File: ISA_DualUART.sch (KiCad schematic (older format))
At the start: 46 parts, among them J1 ISA BUS, J2 ADDR_IRQ, J3 UART1_SEL, J4 UART2_SEL, J5 Serial 1 IDC, J6 Serial 2 IDC, J7 Serial 1 DB9, SW1 GP Address, U1 74LS138, U10 74LS32, U2 74LS138, U3 74LS32, U4 16550, U5 GD75232N, U6 GD75232N, U7 NE558, U8 74LS688, U9 74HC244, X1 1.8432Mhz

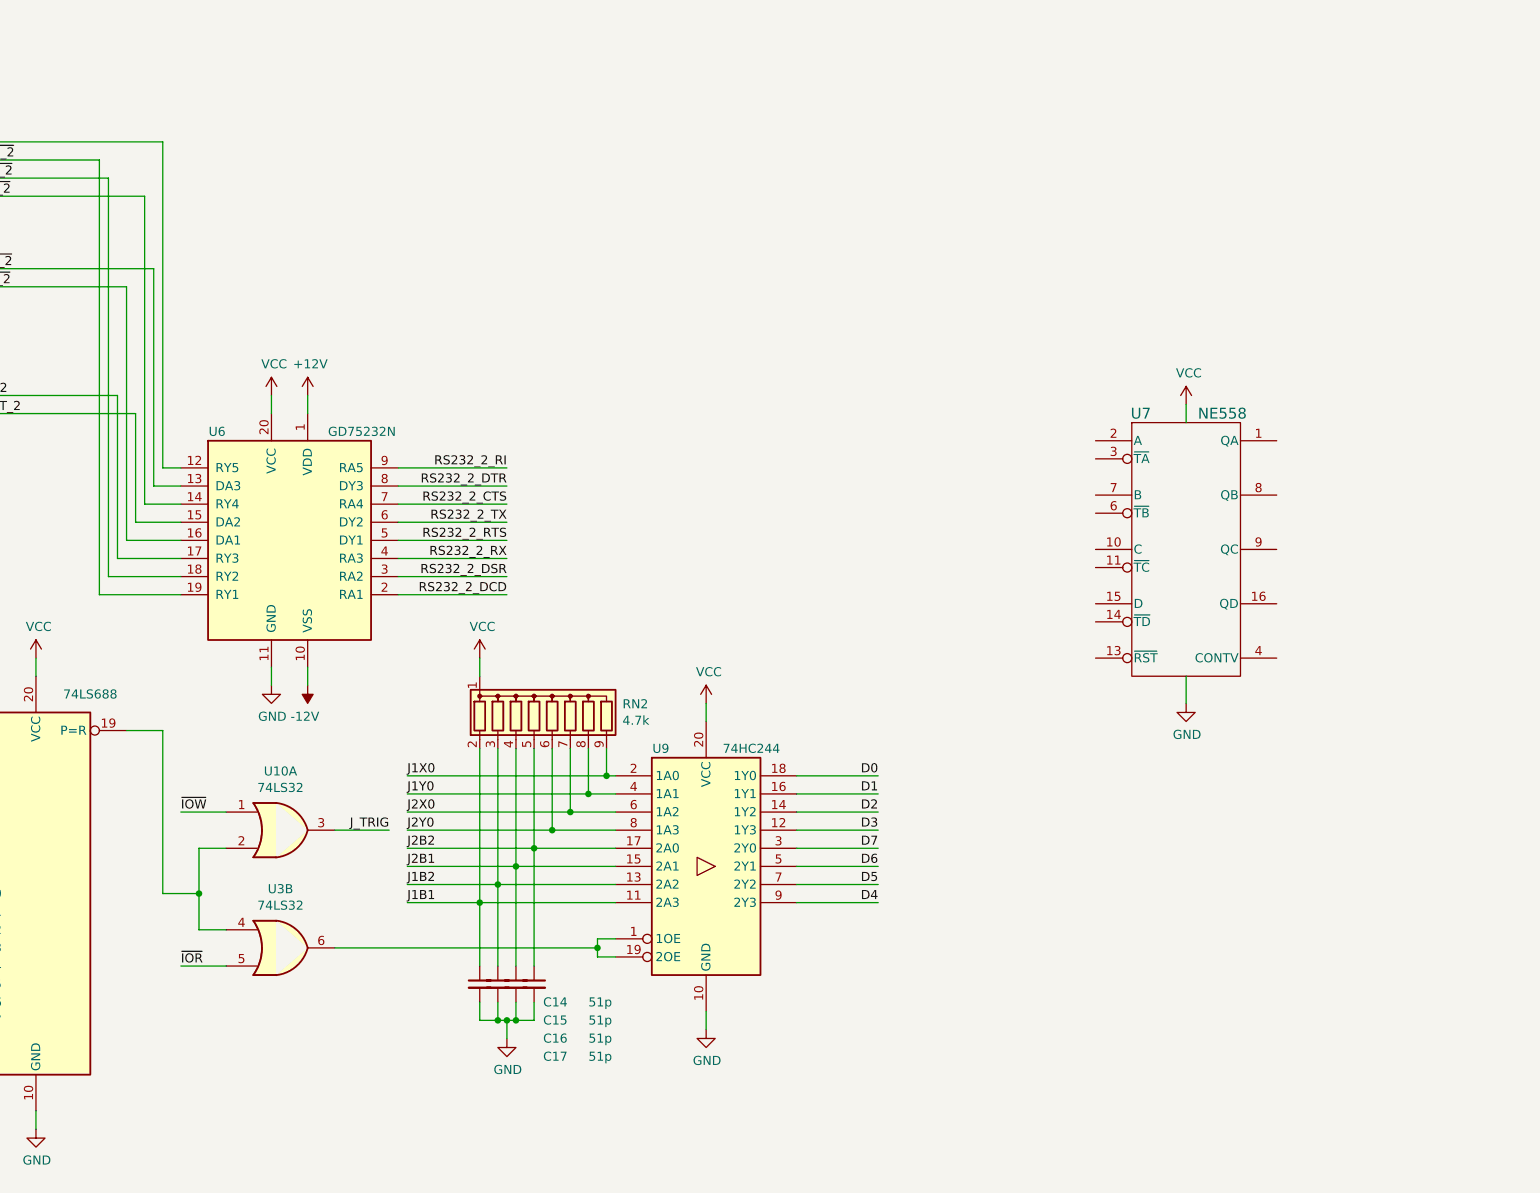
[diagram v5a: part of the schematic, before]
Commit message: Add gameport components
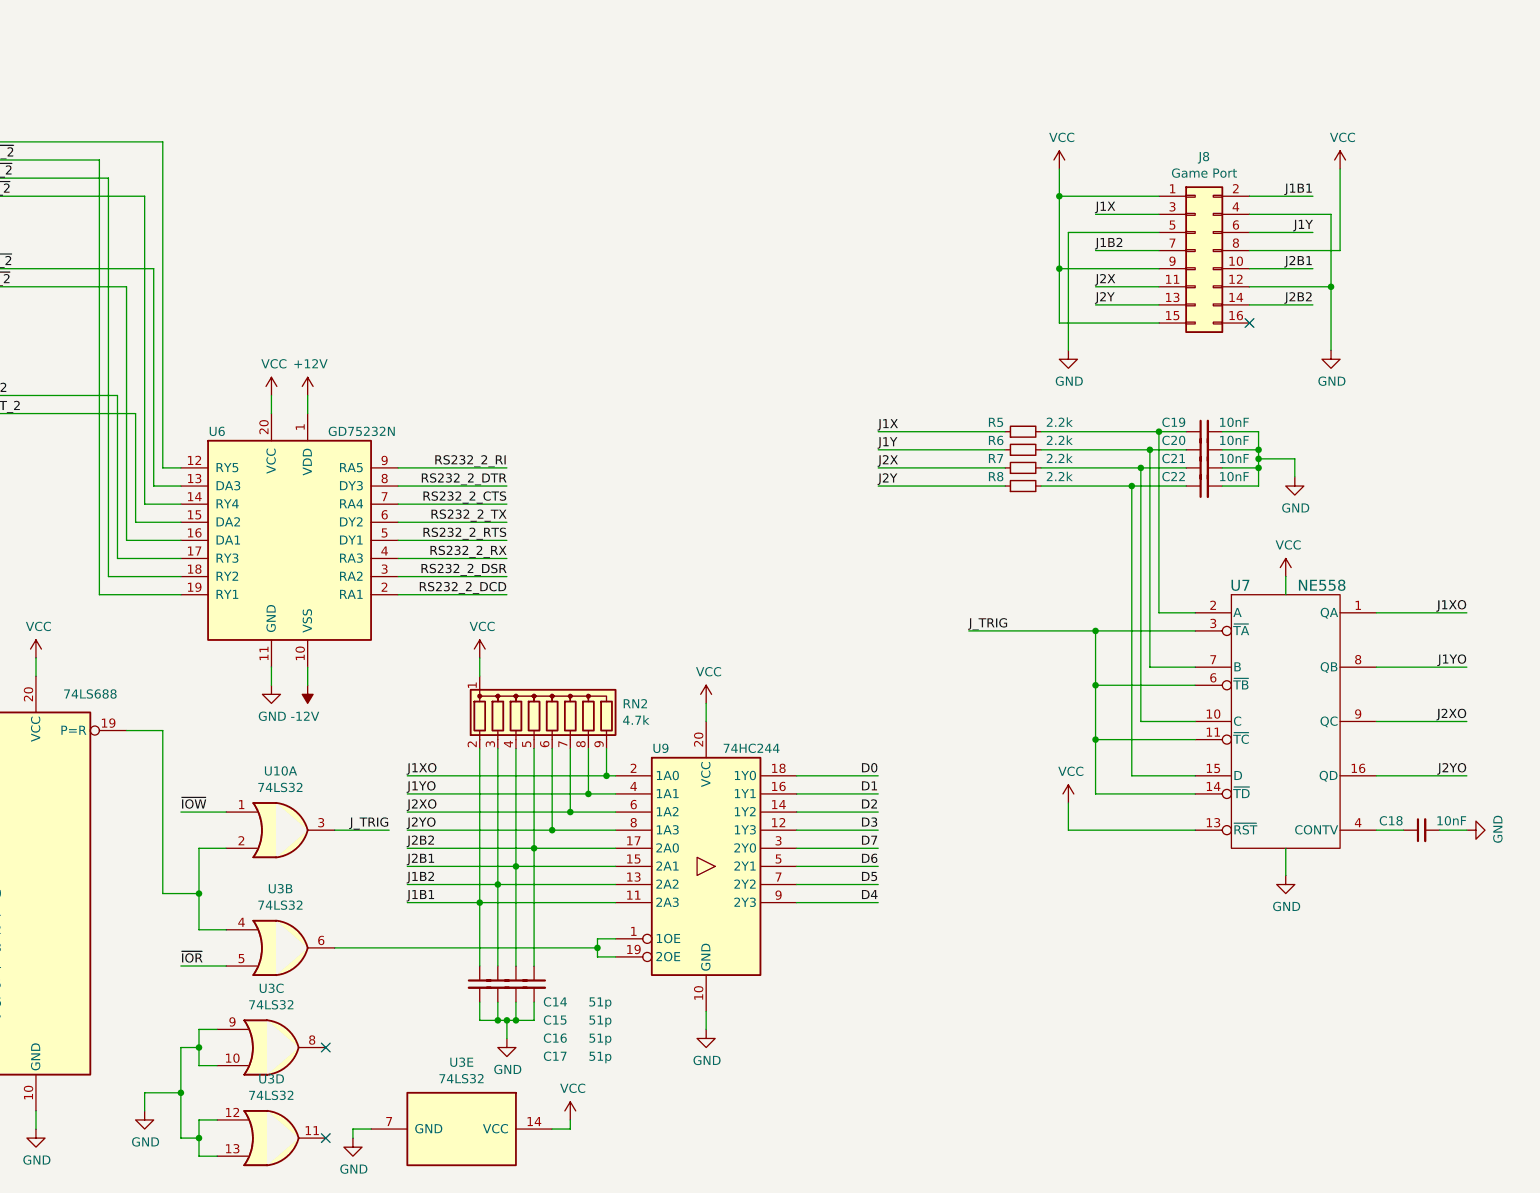
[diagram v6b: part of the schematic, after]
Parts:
- added C18, C19, C20, C21, C22: 10nF, Capacitor_THT:C_Disc_D5.0mm_W2.5mm_P2.50mm, symbol Device:C_Small
- added J8: Game Port, Connector_PinHeader_2.54mm:PinHeader_2x08_P2.54mm_Vertical, symbol Connector_Generic:Conn_02x08_Odd_Even
- added R5, R6, R7, R8: 2.2k, Resistor_THT:R_Axial_DIN0207_L6.3mm_D2.5mm_P10.16mm_Horizontal, symbol Device:R_Small
- added unit 3 of U3
- added unit 4 of U3
- added unit 5 of U3
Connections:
- net J1X0 is gone; now on net J1XO: RN2.9 (R8), U9.2 (1A0)
- net J1Y0 is gone; now on net J1YO: RN2.8 (R7), U9.4 (1A1)
- net J2X0 is gone; now on net J2XO: RN2.7 (R6), U9.6 (1A2)
- net J2Y0 is gone; now on net J2YO: RN2.6 (R5), U9.8 (1A3)
- net GND: now also C18.2, C19.2, C20.2, C21.2, C22.2, J8.12 (Pin_12), J8.4 (Pin_4), J8.5 (Pin_5), U3.10, U3.12, U3.13, U3.7 (GND), U3.9
- net J1B1: now also J8.2 (Pin_2)
- net J1B2: now also J8.7 (Pin_7)
- net J2B1: now also J8.10 (Pin_10)
- net J2B2: now also J8.14 (Pin_14)
- net J_TRIG: now also U7.11 (~TC), U7.14 (~TD), U7.3 (~TA), U7.6 (~TB)
- net VCC: now also U7.13 (~RST), J8.1 (Pin_1), J8.15 (Pin_15), J8.8 (Pin_8), J8.9 (Pin_9), U3.14 (VCC)
- net J1XO: now reaches U7.1 (QA)
- net at U7.10 (C): now also C21.1, R7.2
- net at U7.15 (D): now also C22.1, R8.2
- net J2YO: now reaches U7.16 (QD)
- net at U7.2 (A): now also C19.1, R5.2
- net at U7.4 (CONTV): now also C18.1
- net at U7.7 (B): now also C20.1, R6.2
- net J1YO: now reaches U7.8 (QB)
- net J2XO: now reaches U7.9 (QC)
- new net J1X: J8.3 (Pin_3), R5.1
- new net J1Y: J8.6 (Pin_6), R6.1
- new net J2X: J8.11 (Pin_11), R7.1
- new net J2Y: J8.13 (Pin_13), R8.1
- no-connect marks 39 -> 42
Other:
- moved on the sheet: U7

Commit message: Add more components of the parallel port
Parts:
- added C23, C24, C25, C26: 100nF, Capacitor_THT:C_Disc_D6.0mm_W2.5mm_P5.00mm, symbol Device:C_Small
- added C27, C28, C29, C30, C31, C32, C33, C34, C35: 2.2nF, Capacitor_THT:C_Disc_D5.0mm_W2.5mm_P5.00mm, symbol Device:C_Small
- added JP1: Address selection, Connector_PinHeader_2.54mm:PinHeader_1x02_P2.54mm_Vertical, symbol Device:Jumper_NO_Small
- added JP2: Parport type, Connector_PinHeader_2.54mm:PinHeader_1x03_P2.54mm_Vertical, symbol Device:Jumper_NC_Dual
- added R10, R11, R12, R13, R14, R9: 4.7k, Resistor_THT:R_Axial_DIN0207_L6.3mm_D2.5mm_P10.16mm_Horizontal, symbol Device:R_Small
- added U11: 74LS30, Package_DIP:DIP-14_W7.62mm_LongPads, symbol 74xx:74LS30
- added U12: 74LS86, Package_DIP:DIP-14_W7.62mm_LongPads, symbol 74xx:74LS86
- added U13: 74LS02, Package_DIP:DIP-14_W7.62mm_LongPads, symbol 74xx:74LS02
- added U14: 74LS155, Package_DIP:DIP-16_W7.62mm_LongPads, symbol 74xx:74LS155
- added U15: 74LS245, Package_DIP:DIP-20_W7.62mm_LongPads, symbol 74xx:74LS245
- added U16: 74LS174, Package_DIP:DIP-16_W7.62mm_Socket_LongPads, symbol 74xx:74LS174
- added U17: 74LS374, symbol 74xx:74LS374
- added U18: 74LS05, Package_DIP:DIP-14_W7.62mm_Socket_LongPads, symbol 74xx:74LS05
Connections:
- net A0: now also U14.13 (A0)
- net A1: now also U14.3 (A1)
- net A3: now also U11.3
- net A4: now also U11.4
- net A5: now also U11.5
- net A6: now also U11.6
- net A7: now also U13.5
- net A8: now also U12.5
- net A9: now also U11.11, U11.12
- net AEN: now also U13.6
- net D0: now also U15.18 (B0)
- net D1: now also U15.17 (B1)
- net D2: now also U15.16 (B2)
- net D3: now also U15.15 (B3)
- net D4: now also U15.14 (B4)
- net D5: now also U15.13 (B5)
- net D6: now also U15.12 (B6)
- net D7: now also U15.11 (B7)
- net GND: now also C23.2, C24.2, C25.2, C26.2, C27.2, C28.2, C29.2, C30.2, C31.2, C32.2, C33.2, C34.2, C35.1, JP1.1, JP2.3, U11.7 (GND), U12.7 (GND), U13.7 (GND), U14.2 (Ea2), U14.8 (GND), U15.10 (GND), U15.19 (CE), U16.8 (GND), U17.10 (GND), U18.7 (GND)
- net RESETDRV: now also U13.11, U13.12
- net VCC: now also C23.1, C24.1, C25.1, C26.1, R10.1, R11.1, R12.1, R13.1, R14.1, R9.1, U11.14 (VCC), U12.14 (VCC), U13.14 (VCC), U14.16 (VCC), U15.20 (VCC), U16.16 (VCC), U17.20 (VCC), U18.14 (VCC)
- net ~IOR: now also U13.9
- net ~IOW: now also U14.14 (Eb1)
- new net: U11.1, U13.4
- new net: U11.2, U12.6
- new net: U11.8, U13.8, U14.15 (Eb2)
- new net: JP1.2, R9.2, U12.4
- new net: U16.10 (Q3), U18.9
- new net: U16.2 (Q0), U18.1
- new net: U16.5 (Q1), U18.5
- new net: U16.7 (Q2), U18.3
- new net: JP2.2, U17.1 (OE)
- new net: R12.2, U18.11, U18.4
- new net PARPORT_BD0: U15.2 (A0), U16.3 (D0), U17.18 (D7)
- new net PARPORT_BD1: U15.3 (A1), U16.4 (D1), U17.17 (D6)
- new net PARPORT_BD2: U15.4 (A2), U16.6 (D2), U17.14 (D5)
- new net PARPORT_BD3: U15.5 (A3), U16.11 (D3), U17.13 (D4)
- new net PARPORT_BD4: U15.6 (A4), U16.13 (D4), U17.3 (D0)
- new net PARPORT_BD5: U15.7 (A5), U16.14 (D5), U17.4 (D1)
- new net PARPORT_BD6: U15.8 (A6), U17.7 (D2)
- new net PARPORT_BD7: U15.9 (A7), U17.8 (D3)
- new net PARPORT_DATA0: C34.1, U17.19 (O7)
- new net PARPORT_DATA1: C33.1, U17.16 (O6)
- new net PARPORT_DATA2: C32.1, U17.15 (O5)
- new net PARPORT_DATA3: C31.1, U17.12 (O4)
- new net PARPORT_DATA4: C27.1, U17.2 (O0)
- new net PARPORT_DATA5: C28.1, U17.5 (O1)
- new net PARPORT_DATA6: C29.1, U17.6 (O2)
- new net PARPORT_DATA7: C30.1, U17.9 (O3)
- new net PARPORT_DIR: JP2.1, U16.15 (Q5)
- new net PARPORT_IRQEN: U16.12 (Q4)
- new net PARPORT_R: U13.10, U14.1 (Ea1), U15.1 (A->B)
- new net PARPORT_RPA: U14.7 (Q0a)
- new net PARPORT_RPB: U14.6 (Q1a)
- new net PARPORT_RPC: U14.5 (Q2a)
- new net PARPORT_WPA: U14.9 (Q0b), U17.11 (Cp)
- new net PARPORT_WPC: U14.11 (Q2b), U16.9 (Cp)
- new net ~PARPORT_AUTOFD: R11.2, U18.6
- new net ~PARPORT_INIT: R13.2, U18.10
- new net ~PARPORT_RESET: U13.13, U16.1 (~Mr)
- new net ~PARPORT_SLCTIN: R14.2, U18.8
- new net ~PARPORT_STROBE: C35.2, R10.2, U18.2
- no-connect marks 42 -> 45
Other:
- note added: "Closed - 0x278/9/A\nOpen - 0x378/9/A"
- note added: "Gameport"
- note added: "ISA & Decoupling"
- note added: "Serial Ports"
- moved on the sheet: C1, C10, C11, C14, C15, C16, C17, C18, C19, C2, C20, C21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

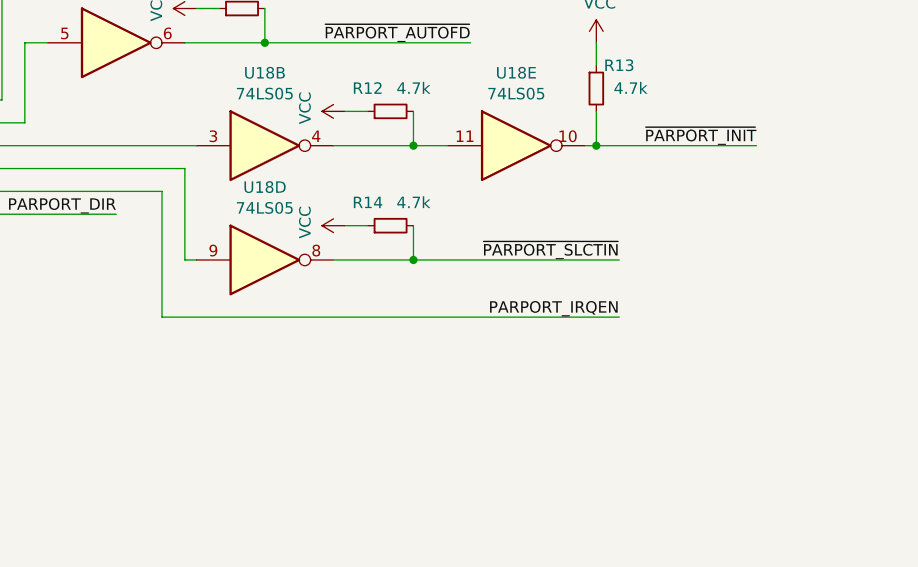
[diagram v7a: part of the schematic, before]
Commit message: More components of the parallel port
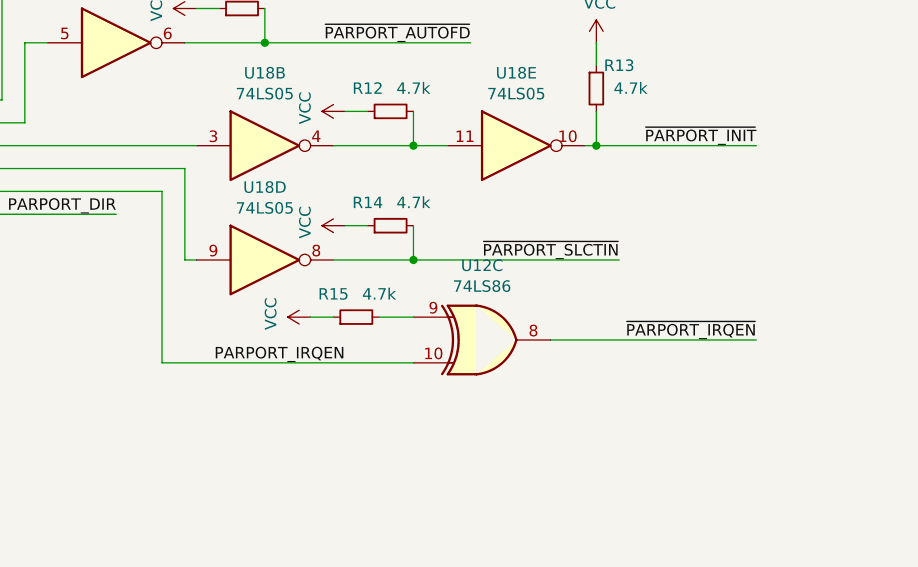
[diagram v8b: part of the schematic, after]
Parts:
- added R15: 4.7k, Resistor_THT:R_Axial_DIN0207_L6.3mm_D2.5mm_P10.16mm_Horizontal, symbol Device:R_Small
- added unit 3 of U12
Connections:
- net PARPORT_IRQEN: now also U12.10
- net VCC: now also R15.1
- new net: R15.2, U12.9
- new net ~PARPORT_IRQEN: U12.8
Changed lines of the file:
@@
 Wire Wire Line
 	17100 12100 17950 12100
+Text Label 18750 12850 2    50   ~ 0
+PARPORT_IRQEN
+$Comp
+L 74xx:74LS86 U12
+U 3 1 6AD8D7C0
+P 19350 12750
+F 0 "U12" H 19350 13075 50  0000 C CNN
+F 1 "74LS86" H 19350 12984 50  0000 C CNN
+F 2 "Package_DIP:DIP-14_W7.62mm_LongPads" H 19350 12750 50  0001 C CNN
+F 3 "74xx/74ls86.pdf" H 19350 12750 50  0001 C CNN
+	3    19350 12750
+	1    0    0    -1
+$EndComp
 Wire Wire Line
-	17950 12100 17950 12650
+	17950 12850 19050 12850
 Wire Wire Line
-	17950 12650 19950 12650
-Text Label 19950 12650 2    50   ~ 0
-PARPORT_IRQEN
+	17950 12100 17950 12850
+$Comp
+L Device:R_Small R15
+U 1 1 6AE51D98
+P 18800 12650
+F 0 "R15" V 18900 12750 50  0000 C CNN
+F 1 "4.7k" V 18900 12550 50  0000 C CNN
+F 2 "Resistor_THT:R_Axial_DIN0207_L6.3mm_D2.5mm_P10.16mm_Horizontal" H 18800 12650 50  0001 C CNN
+F 3 "~" H 18800 12650 50  0001 C CNN
+	1    18800 12650
+	0    -1   -1   0
+$EndComp
+Wire Wire Line
+	18900 12650 19050 12650
+$Comp
+L power:VCC #PWR?
+U 1 1 6AEFBB1A
+P 18600 12650
+F 0 "#PWR?" H 18600 12500 50  0001 C CNN
+F 1 "VCC" H 18615 12823 50  0000 C CNN
+F 2 "" H 18600 12650 50  0001 C CNN
+F 3 "" H 18600 12650 50  0001 C CNN
+	1    18600 12650
+	0    -1   -1   0
+$EndComp
+Wire Wire Line
+	18600 12650 18700 12650
+Wire Wire Line
+	19650 12750 20550 12750
 Wire Bus Line
 	15400 9100 15400 13500
+Text Label 20550 12750 2    50   ~ 0
+~PARPORT_IRQEN
 $EndSCHEMATC
